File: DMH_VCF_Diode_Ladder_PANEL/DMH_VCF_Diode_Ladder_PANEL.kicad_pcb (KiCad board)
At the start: 2 copper layers, 100 x 200 mm, 5 parts, among them J0 Panel_GND_Solder_Wire_Pad

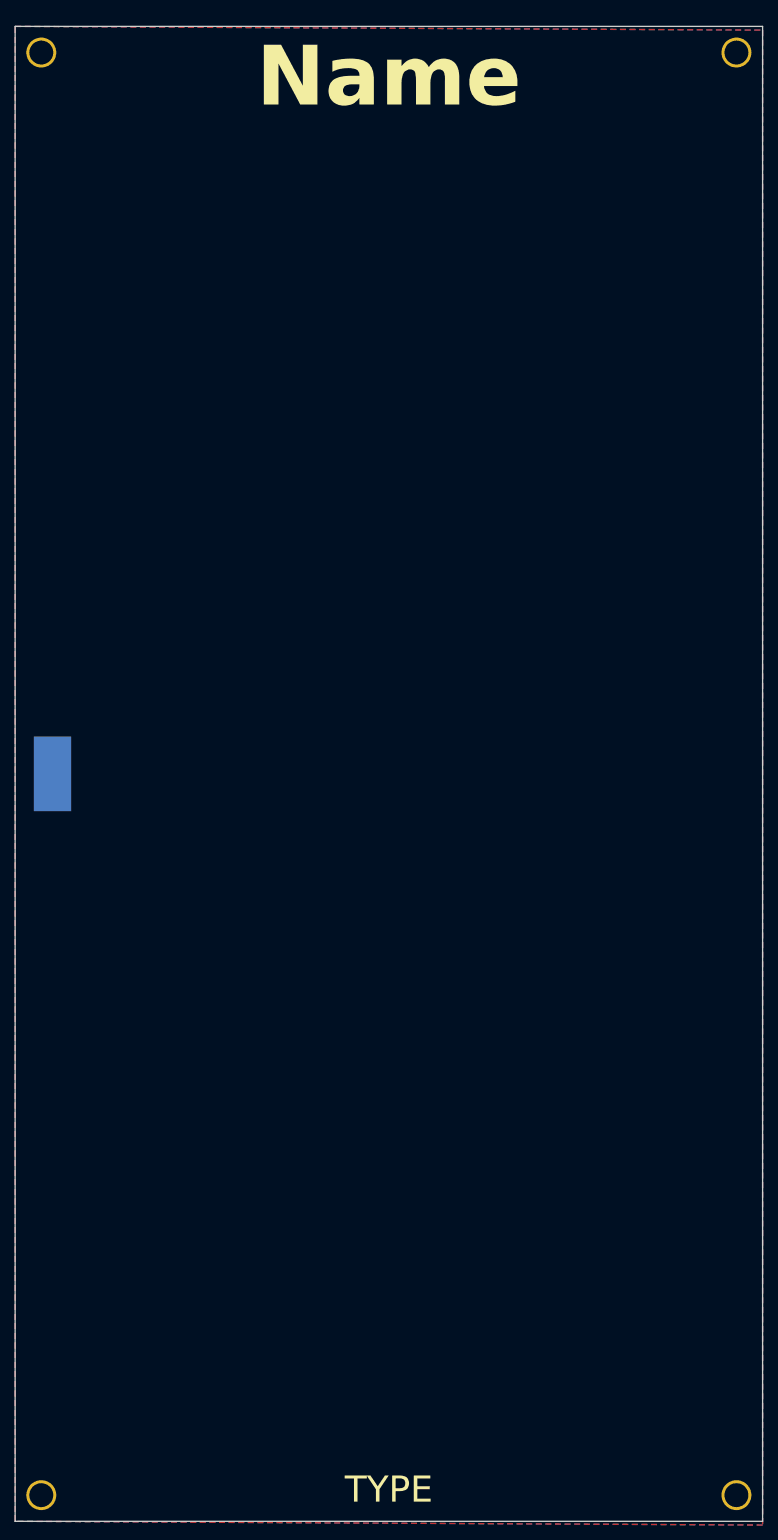
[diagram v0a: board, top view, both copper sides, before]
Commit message: Designed front panel
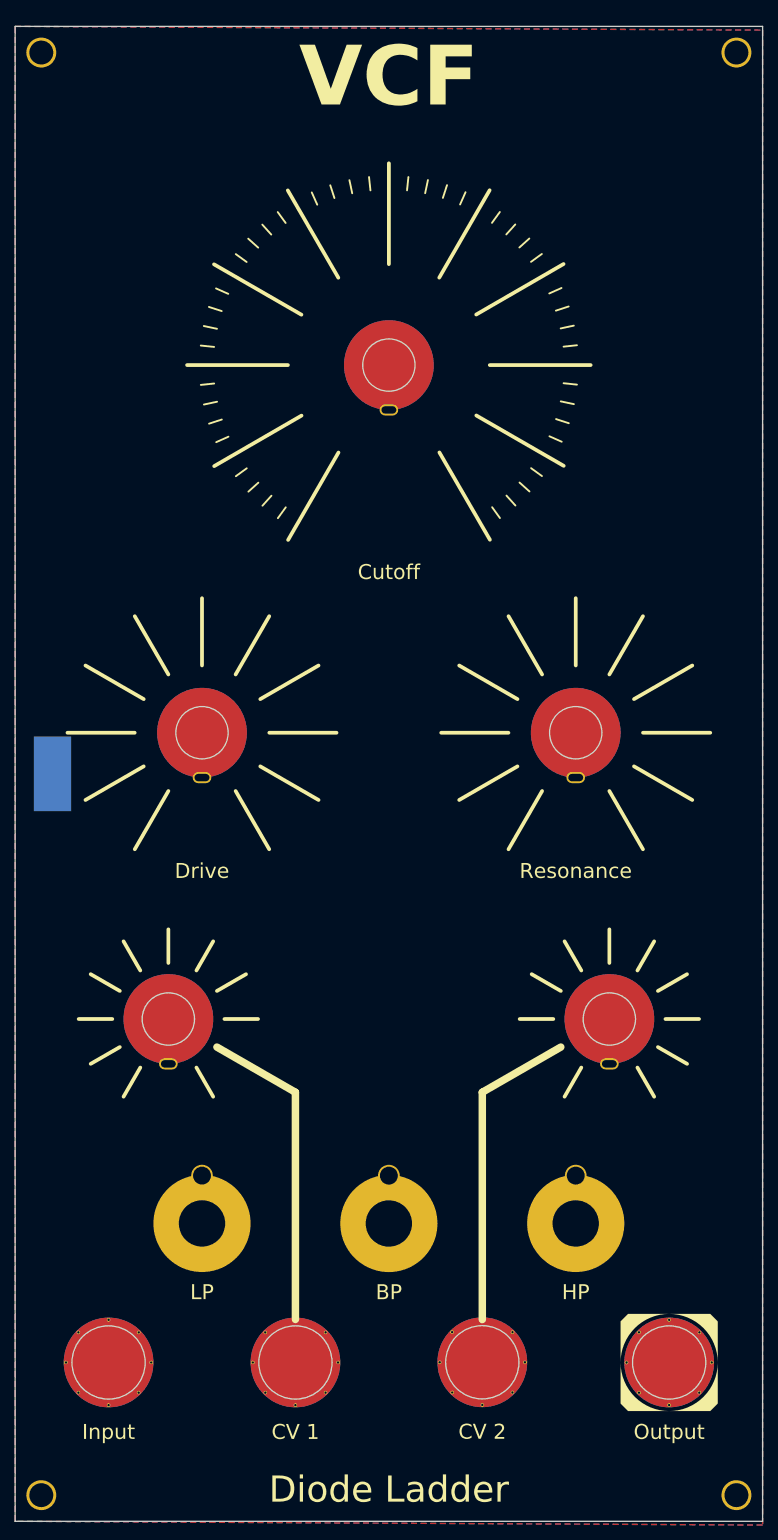
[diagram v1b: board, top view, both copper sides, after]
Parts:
- added H10: Drive, SynthStuff:Pot_Cutout_Medium, F.Cu at (75.0, 124.5)
- added H11: Resonance, SynthStuff:Pot_Cutout_Medium, F.Cu at (125.0, 124.5)
- added H12: CV 1 Amount, SynthStuff:Pot_Cutout_Tiny, F.Cu at (70.5, 162.8)
- added H13: CV 2 Amount, SynthStuff:Pot_Cutout_Tiny, F.Cu at (129.5, 162.8)
- added H14: LP, SynthStuff:Toggle_Switch_Cutout, F.Cu at (75.0, 190.2)
- added H15: BP, SynthStuff:Toggle_Switch_Cutout, F.Cu at (100.0, 190.2)
- added H16: HP, SynthStuff:Toggle_Switch_Cutout, F.Cu at (125.0, 190.2)
- added H5: Input, SynthStuff:Jack_6.35mm_Cutout_v3, F.Cu at (62.5, 208.8)
- added H6: CV 1, SynthStuff:Jack_6.35mm_Cutout_v3, F.Cu at (87.5, 208.8)
- added H7: CV 2, SynthStuff:Jack_6.35mm_Cutout_v3, F.Cu at (112.5, 208.7)
- added H8: Output, SynthStuff:Jack_6.35mm_Cutout_Output_v6, F.Cu at (137.5, 208.8)
- added H9: Cutoff, SynthStuff:Pot_Cutout_Huge_v2, F.Cu at (100.0, 75.3)
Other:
- board text added: "Diode Ladder"
- board text added: "VCF"
- board text removed: "Name"
- board text removed: "TYPE"

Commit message: Main schematic in progress
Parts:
- added H17: Bus CV Amount, SynthStuff:Pot_Cutout_Tiny, F.Cu at (100.0, 152.0)

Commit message: Finished schematic and added Bus CV 2 pot
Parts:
- added H18: CV 2, SynthStuff:Jack_6.35mm_Cutout_v3, F.Cu at (100.0, 208.7)
- H13: value CV 2 Amount -> CV 3 Amount
- H17: value Bus CV Amount -> (Bus) CV 2 Amt
- H7: value CV 2 -> CV 3
- moved H17 10.8 mm to (100.0, 162.8)
- moved H7 6.25 mm to (118.8, 208.8)
- moved H6 6.25 mm to (81.2, 208.8)
- moved H14 4.50 mm to (70.5, 190.0)
- moved H16 4.50 mm to (129.5, 190.2)
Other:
- board text added: "(Bus) CV 2"
- board text added: "CV 1"
- board text added: "CV 3"

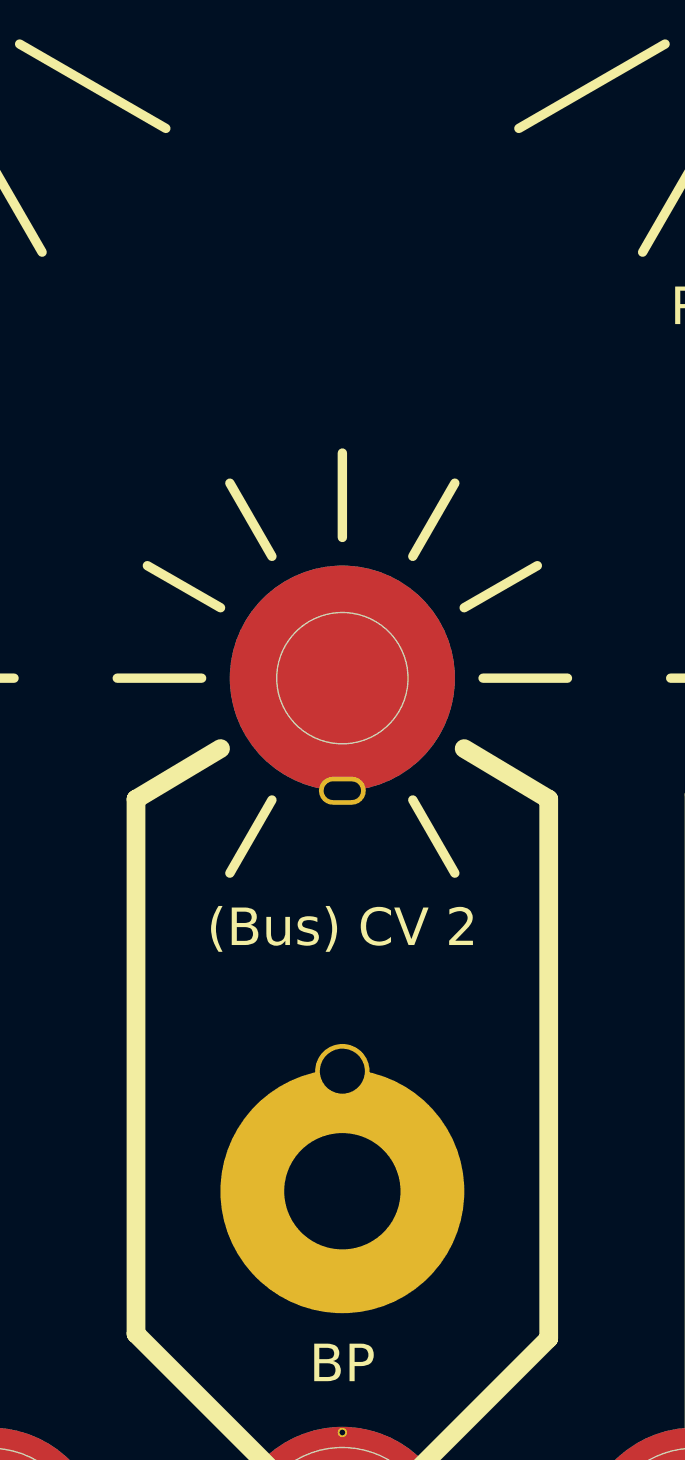
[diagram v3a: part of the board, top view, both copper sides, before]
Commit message: Added Bus CV On Off switch
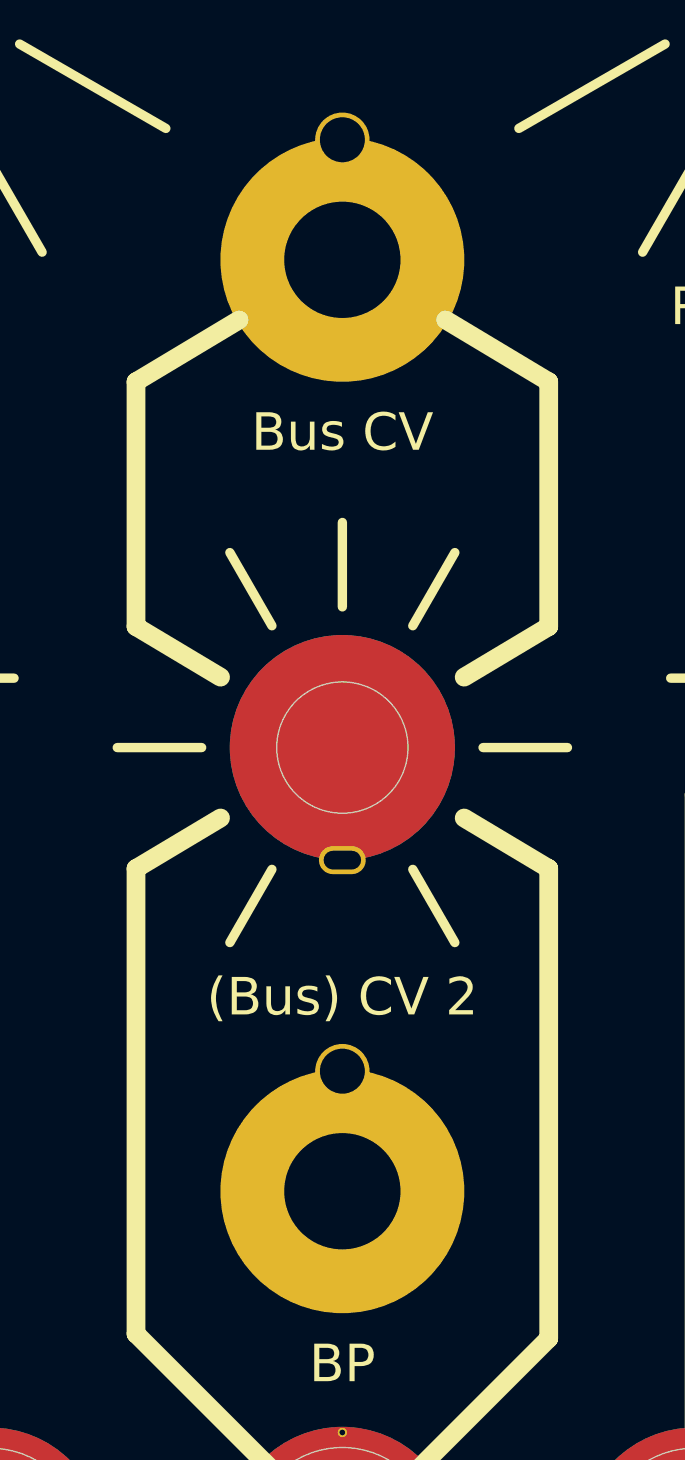
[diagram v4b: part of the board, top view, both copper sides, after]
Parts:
- added H19: Bus CV, SynthStuff:Toggle_Switch_Cutout, F.Cu at (100.0, 140.5)
- H17: value (Bus) CV 2 Amt -> (Bus) CV 2 Amount
- moved H17 3.70 mm to (100.0, 166.5)
